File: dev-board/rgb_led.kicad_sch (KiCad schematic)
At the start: 1 part

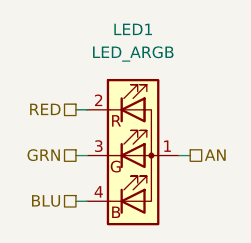
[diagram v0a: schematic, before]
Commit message: created dev-board to prove design before full-size
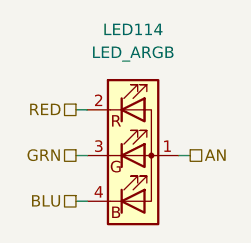
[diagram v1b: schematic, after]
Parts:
- renumbered LED1 to LED114
